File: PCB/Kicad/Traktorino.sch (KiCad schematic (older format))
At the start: 86 parts, among them J1 analog_pins, J2 mux_pins, J3 595_pins, J4 d13

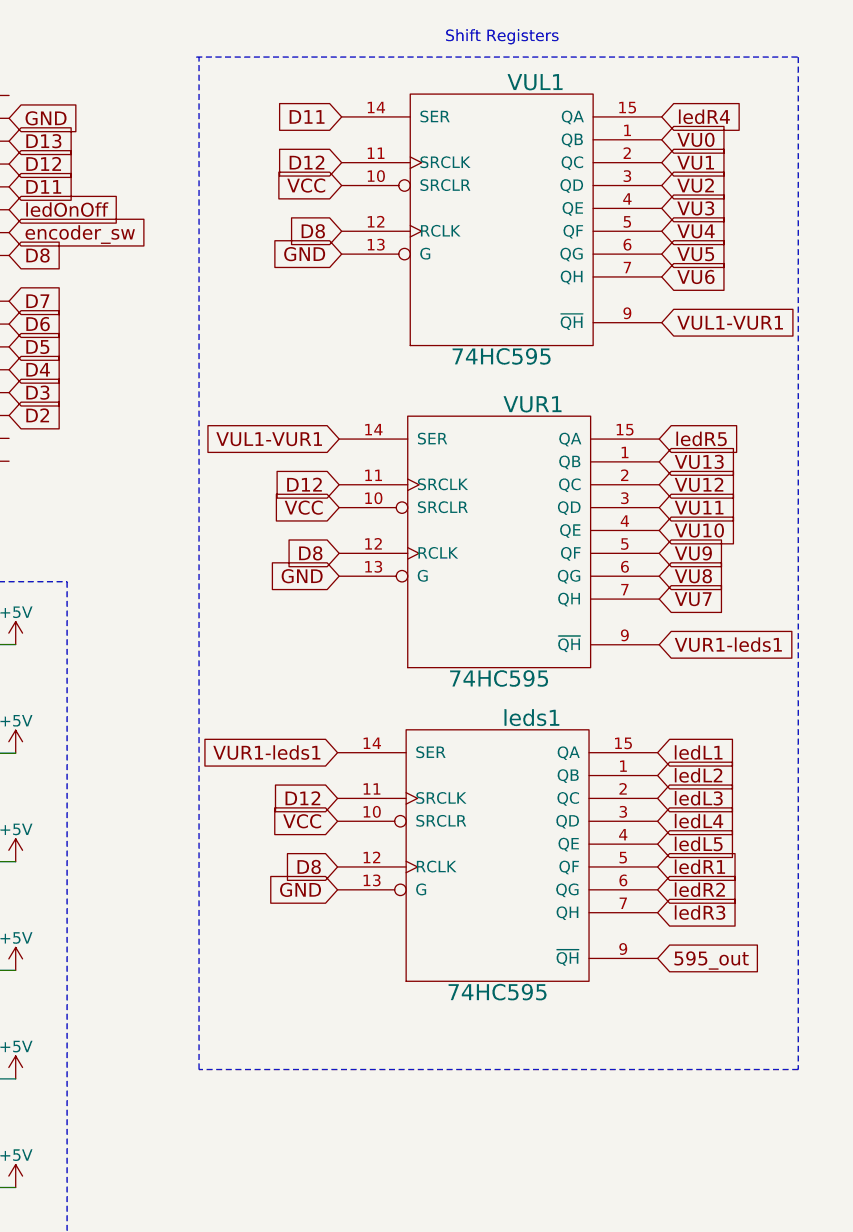
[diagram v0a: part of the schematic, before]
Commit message: SHIFT REGS
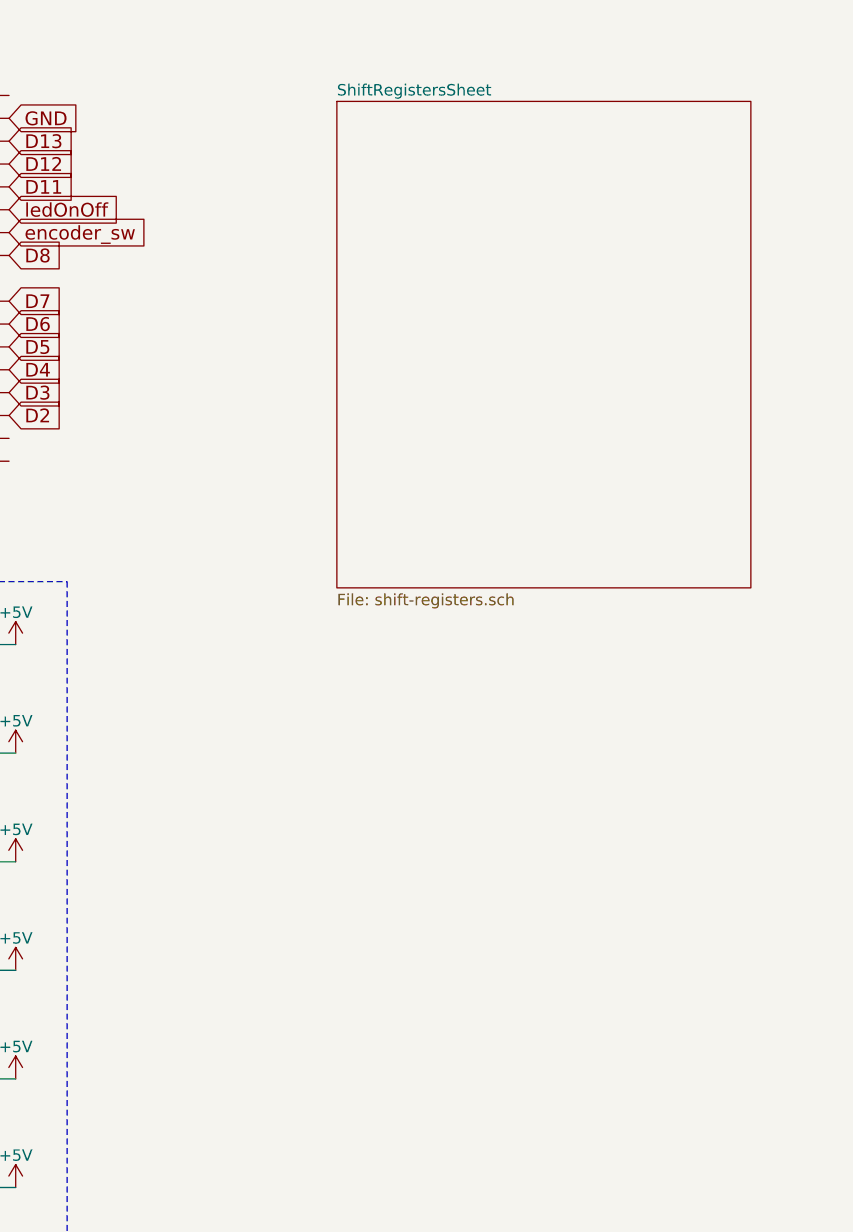
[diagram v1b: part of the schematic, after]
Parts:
- removed VUL1, VUR1, leds1: 74HC595, 74HC595:DIL16, symbol Traktorino-rescue:74HC595
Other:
- note removed: "Shift Registers"
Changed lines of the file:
@@
 $Descr A4 11693 8268
 encoding utf-8
-Sheet 1 1
+Sheet 1 2
 Title ""
 Date ""
@@
 Text GLabel 4575 6450 2    60   Input ~ 0
 Bshift
-Text GLabel 10451 1067 2    60   Input ~ 0
-VU0
-Text GLabel 10440 2976 2    60   Input ~ 0
-VU8
-Text GLabel 10440 3076 2    60   Input ~ 0
-VU7
-Text GLabel 10451 1167 2    60   Input ~ 0
-VU1
-Text GLabel 10451 1267 2    60   Input ~ 0
-VU2
-Text GLabel 10451 1367 2    60   Input ~ 0
-VU3
-Text GLabel 10451 1467 2    60   Input ~ 0
-VU4
-Text GLabel 10451 1567 2    60   Input ~ 0
-VU5
-Text GLabel 10451 1667 2    60   Input ~ 0
-VU6
-Text GLabel 10440 2876 2    60   Input ~ 0
-VU9
-Text GLabel 10440 2776 2    60   Input ~ 0
-VU10
-Text GLabel 10440 2676 2    60   Input ~ 0
-VU11
-Text GLabel 10440 2576 2    60   Input ~ 0
-VU12
-Text GLabel 10440 2476 2    60   Input ~ 0
-VU13
-Text GLabel 10433 3748 2    60   Input ~ 0
-ledL1
-Text GLabel 10433 3848 2    60   Input ~ 0
-ledL2
-Text GLabel 10433 3948 2    60   Input ~ 0
-ledL3
-Text GLabel 10433 4048 2    60   Input ~ 0
-ledL4
-Text GLabel 10433 4148 2    60   Input ~ 0
-ledL5
-Text GLabel 10433 4248 2    60   Input ~ 0
-ledR1
-Text GLabel 10433 4348 2    60   Input ~ 0
-ledR2
-Text GLabel 10433 4448 2    60   Input ~ 0
-ledR3
-Text GLabel 10451 967  2    60   Input ~ 0
-ledR4
-Text GLabel 10440 2376 2    60   Input ~ 0
-ledR5
-Text GLabel 9033 4348 0    60   Input ~ 0
-GND
-Text GLabel 9051 1467 0    60   Input ~ 0
-D8
-Text GLabel 9051 967  0    60   Input ~ 0
-D11
-Text GLabel 9051 1267 0    60   Input ~ 0
-VCC
-Text GLabel 9051 1567 0    60   Input ~ 0
-GND
 $Comp
 L Traktorino-rescue:ARDUINO_SHIELD SHIELD1
@@
 Text GLabel 5875 6850 2    60   Input ~ 0
 encoder_sw
-$Comp
-L Traktorino-rescue:74HC595 leds1
-U 1 1 5975AEC7
-P 9733 4198
-F 0 "leds1" H 9883 4798 70  0000 C CNN
-F 1 "74HC595" H 9733 3598 70  0000 C CNN
-F 2 "74HC595:DIL16" H 9733 4198 60  0001 C CNN
-F 3 "" H 9733 4198 60  0000 C CNN
-	1    9733 4198
-	1    0    0    -1
-$EndComp
-Text GLabel 9033 4248 0    60   Input ~ 0
-D8
-Text GLabel 9051 1167 0    60   Input ~ 0
-D12
-Text GLabel 9033 3948 0    60   Input ~ 0
-D12
 Text GLabel 7596 1173 2    60   Input ~ 0
 D12
-Text GLabel 9033 4048 0    60   Input ~ 0
-VCC
 Text GLabel 5696 2173 0    60   Input ~ 0
 A2
@@
 Text GLabel 5696 2473 0    60   Input ~ 0
 A5
-Text GLabel 10433 4648 2    60   Input ~ 0
-595_out
 $Comp
 L Traktorino-rescue:CONN_01X06 J2
@@
 	1    0    0    -1
 $EndComp
-Text GLabel 9040 2976 0    60   Input ~ 0
-GND
-Text GLabel 9040 2876 0    60   Input ~ 0
-D8
-Text GLabel 9040 2576 0    60   Input ~ 0
-D12
-Text GLabel 9040 2676 0    60   Input ~ 0
-VCC
 $Comp
 L Traktorino-rescue:CONN_01X07 J1
@@
 Text Notes 1750 625  0    50   ~ 0
 Multiplexers
-Text GLabel 10451 1867 2    60   Input ~ 0
-VUL1-VUR1
-Text GLabel 9040 2376 0    60   Input ~ 0
-VUL1-VUR1
-Text GLabel 10440 3276 2    60   Input ~ 0
-VUR1-leds1
-Text GLabel 9033 3748 0    60   Input ~ 0
-VUR1-leds1
-Wire Notes Line
-	8415 705  11048 705
-Wire Notes Line
-	11048 705  11048 5134
-Wire Notes Line
-	11048 5134 8427 5134
-Wire Notes Line
-	8427 5134 8427 705
-Text Notes 9503 651  0    50   ~ 0
-Shift Registers
 $Comp
 L Traktorino-rescue:SW_PUSH_SMALL BL2
@@
 Text GLabel 7596 1473 2    60   Input ~ 0
 encoder_sw
-$Comp
-L Traktorino-rescue:74HC595 VUL1
-U 1 1 59743C7D
-P 9751 1417
-F 0 "VUL1" H 9901 2017 70  0000 C CNN
-F 1 "74HC595" H 9751 817 70  0000 C CNN
-F 2 "74HC595:DIL16" H 9751 1417 60  0001 C CNN
-F 3 "" H 9751 1417 60  0000 C CNN
-	1    9751 1417
-	1    0    0    -1
-$EndComp
-$Comp
-L Traktorino-rescue:74HC595 VUR1
-U 1 1 597578F3
-P 9740 2826
-F 0 "VUR1" H 9890 3426 70  0000 C CNN
-F 1 "74HC595" H 9740 2226 70  0000 C CNN
-F 2 "74HC595:DIL16" H 9740 2826 60  0001 C CNN
-F 3 "" H 9740 2826 60  0000 C CNN
-	1    9740 2826
-	1    0    0    -1
-$EndComp
+$Sheet
+S 9030 899  1811 2128
+U 605D0BAE
+F0 "ShiftRegistersSheet" 50
+F1 "shift-registers.sch" 50
+$EndSheet
 $EndSCHEMATC

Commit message: SCHEMA UPD
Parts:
- removed MUXbuttons1, MUXpots1: 4067D, 40xx:40xx-DIL24-6, symbol Traktorino-rescue:4067D-RESCUE-DJ_0
- added SW?: SW_Push, symbol Switch:SW_Push
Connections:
- net GND: now also SW?.1
- new net SWPLAY-L: SW?.2
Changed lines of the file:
@@
 $Descr A4 11693 8268
 encoding utf-8
-Sheet 1 2
+Sheet 1 3
 Title ""
 Date ""
@@
 	1    5450 2950
 	1    0    0    -1
-$EndComp
-$Comp
-L Traktorino-rescue:4067D-RESCUE-DJ_0 MUXpots1
-U 1 1 578962B0
-P 1350 2075
-F 0 "MUXpots1" H 1050 3200 50  0000 L BNN
-F 1 "4067D" H 1050 775 50  0000 L BNN
-F 2 "40xx:40xx-DIL24-6" H 1350 2225 50  0001 C CNN
-F 3 "" H 1350 2075 60  0000 C CNN
-	1    1350 2075
-	-1   0    0    1
 $EndComp
 Text GLabel 1754 5416 2    60   Input ~ 0
@@
 Text Notes 1700 3600 0    50   ~ 0
 Vumeter
-$Comp
-L Traktorino-rescue:4067D-RESCUE-DJ_0 MUXbuttons1
-U 1 1 579016CB
-P 3050 2075
-F 0 "MUXbuttons1" H 2750 3200 50  0000 L BNN
-F 1 "4067D" H 2750 775 50  0000 L BNN
-F 2 "40xx:40xx-DIL24-6" H 3050 2225 50  0001 C CNN
-F 3 "" H 3050 2075 60  0000 C CNN
-	1    3050 2075
-	-1   0    0    1
-$EndComp
 Wire Notes Line
 	550  675  3850 675
-Wire Notes Line
-	3850 675  3850 3475
 Wire Notes Line
 	3850 3475 550  3475
@@
 Text Notes 5675 6300 0    50   ~ 0
 Browse encoder
-Text GLabel 2550 1575 0    60   Input ~ 0
-GND
-Text GLabel 2550 1725 0    60   Input ~ 0
-VCC
-Text GLabel 1850 2475 2    60   Input ~ 0
-potCF
-Text GLabel 1850 2375 2    60   Input ~ 0
-potL1
-Text GLabel 1850 2275 2    60   Input ~ 0
-potL2
-Text GLabel 1850 2175 2    60   Input ~ 0
-potL3
-Text GLabel 1850 1875 2    60   Input ~ 0
-potL6
-Text GLabel 1850 1975 2    60   Input ~ 0
-potL5
-Text GLabel 1850 2075 2    60   Input ~ 0
-potL4
-Text GLabel 1850 2675 2    60   Input ~ 0
-D7
-Text GLabel 850  1575 0    60   Input ~ 0
-GND
-Text GLabel 850  1725 0    60   Input ~ 0
-VCC
-Text GLabel 850  2475 0    60   Input ~ 0
-A0
-Text GLabel 1850 3075 2    60   Input ~ 0
-GND
-Text GLabel 1850 2975 2    60   Input ~ 0
-D4
-Text GLabel 1850 2775 2    60   Input ~ 0
-D6
-Text GLabel 1850 2875 2    60   Input ~ 0
-D5
-Text GLabel 1850 1775 2    60   Input ~ 0
-potL7
-Text GLabel 1850 1675 2    60   Input ~ 0
-potMain
-Text GLabel 1850 1575 2    60   Input ~ 0
-potR7
-Text GLabel 1850 1475 2    60   Input ~ 0
-potR6
-Text GLabel 1850 1375 2    60   Input ~ 0
-potR5
-Text GLabel 1850 1275 2    60   Input ~ 0
-potR4
-Text GLabel 1850 1175 2    60   Input ~ 0
-potR3
-Text GLabel 1850 1075 2    60   Input ~ 0
-potR2
-Text GLabel 1850 975  2    60   Input ~ 0
-potR1
-Text GLabel 2550 2475 0    60   Input ~ 0
-A1
-Text GLabel 3550 2675 2    60   Input ~ 0
-D7
-Text GLabel 3550 2775 2    60   Input ~ 0
-D6
-Text GLabel 3550 2875 2    60   Input ~ 0
-D5
-Text GLabel 3550 2975 2    60   Input ~ 0
-D4
-Text GLabel 3550 3075 2    60   Input ~ 0
-GND
-Text GLabel 3550 2475 2    60   Input ~ 0
-BL1
-Text GLabel 3550 2375 2    60   Input ~ 0
-BL2
-Text GLabel 3550 2275 2    60   Input ~ 0
-BL3
-Text GLabel 3550 2175 2    60   Input ~ 0
-BL4
-Text GLabel 3550 2075 2    60   Input ~ 0
-BL5
-Text GLabel 3550 1975 2    60   Input ~ 0
-BL6
-Text GLabel 3550 1575 2    60   Input ~ 0
-Bshift
-Text GLabel 3550 1475 2    60   Input ~ 0
-BR6
-Text GLabel 3550 1375 2    60   Input ~ 0
-BR5
-Text GLabel 3550 1275 2    60   Input ~ 0
-BR4
-Text GLabel 3550 1175 2    60   Input ~ 0
-BR3
-Text GLabel 3550 1075 2    60   Input ~ 0
-BR2
-Text GLabel 3550 975  2    60   Input ~ 0
-BR1
 Text GLabel 4650 900  0    60   Input ~ 0
 GND
@@
 F1 "shift-registers.sch" 50
 $EndSheet
+$Comp
+L Switch:SW_Push SW?
+U 1 1 605E95CD
+P 4400 7400
+F 0 "SW?" H 4400 7685 50  0000 C CNN
+F 1 "SW_Push" H 4400 7594 50  0000 C CNN
+F 2 "" H 4400 7600 50  0001 C CNN
+F 3 "~" H 4400 7600 50  0001 C CNN
+	1    4400 7400
+	1    0    0    -1
+$EndComp
+$Comp
+L power:GND #PWR?
+U 1 1 605F7A1F
+P 4100 7400
+F 0 "#PWR?" H 4100 7150 50  0001 C CNN
+F 1 "GND" H 4105 7227 50  0000 C CNN
+F 2 "" H 4100 7400 50  0001 C CNN
+F 3 "" H 4100 7400 50  0001 C CNN
+	1    4100 7400
+	1    0    0    -1
+$EndComp
+Wire Wire Line
+	4200 7400 4100 7400
+Text GLabel 4600 7400 2    40   Input ~ 0
+SWPLAY-L
+$Sheet
+S 9050 3700 1650 1450
+U 60600FDB
+F0 "MultiplexersSheet" 40
+F1 "multiplexers.sch" 40
+$EndSheet
 $EndSCHEMATC

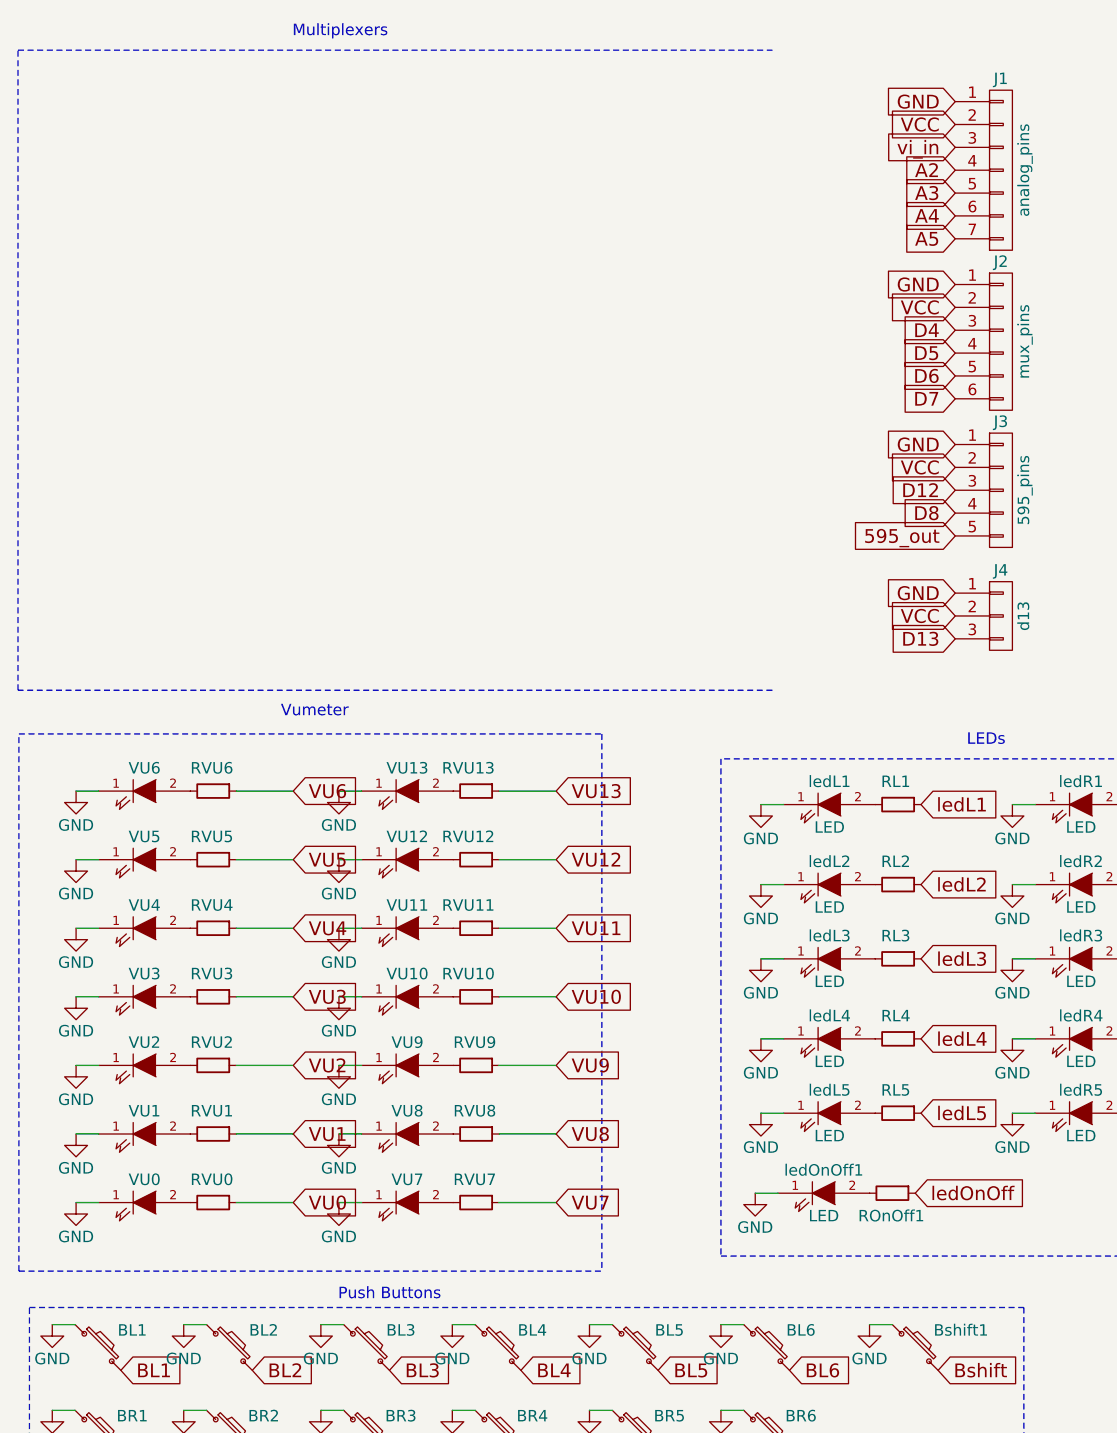
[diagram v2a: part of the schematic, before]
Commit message: multiplexers and vumeters
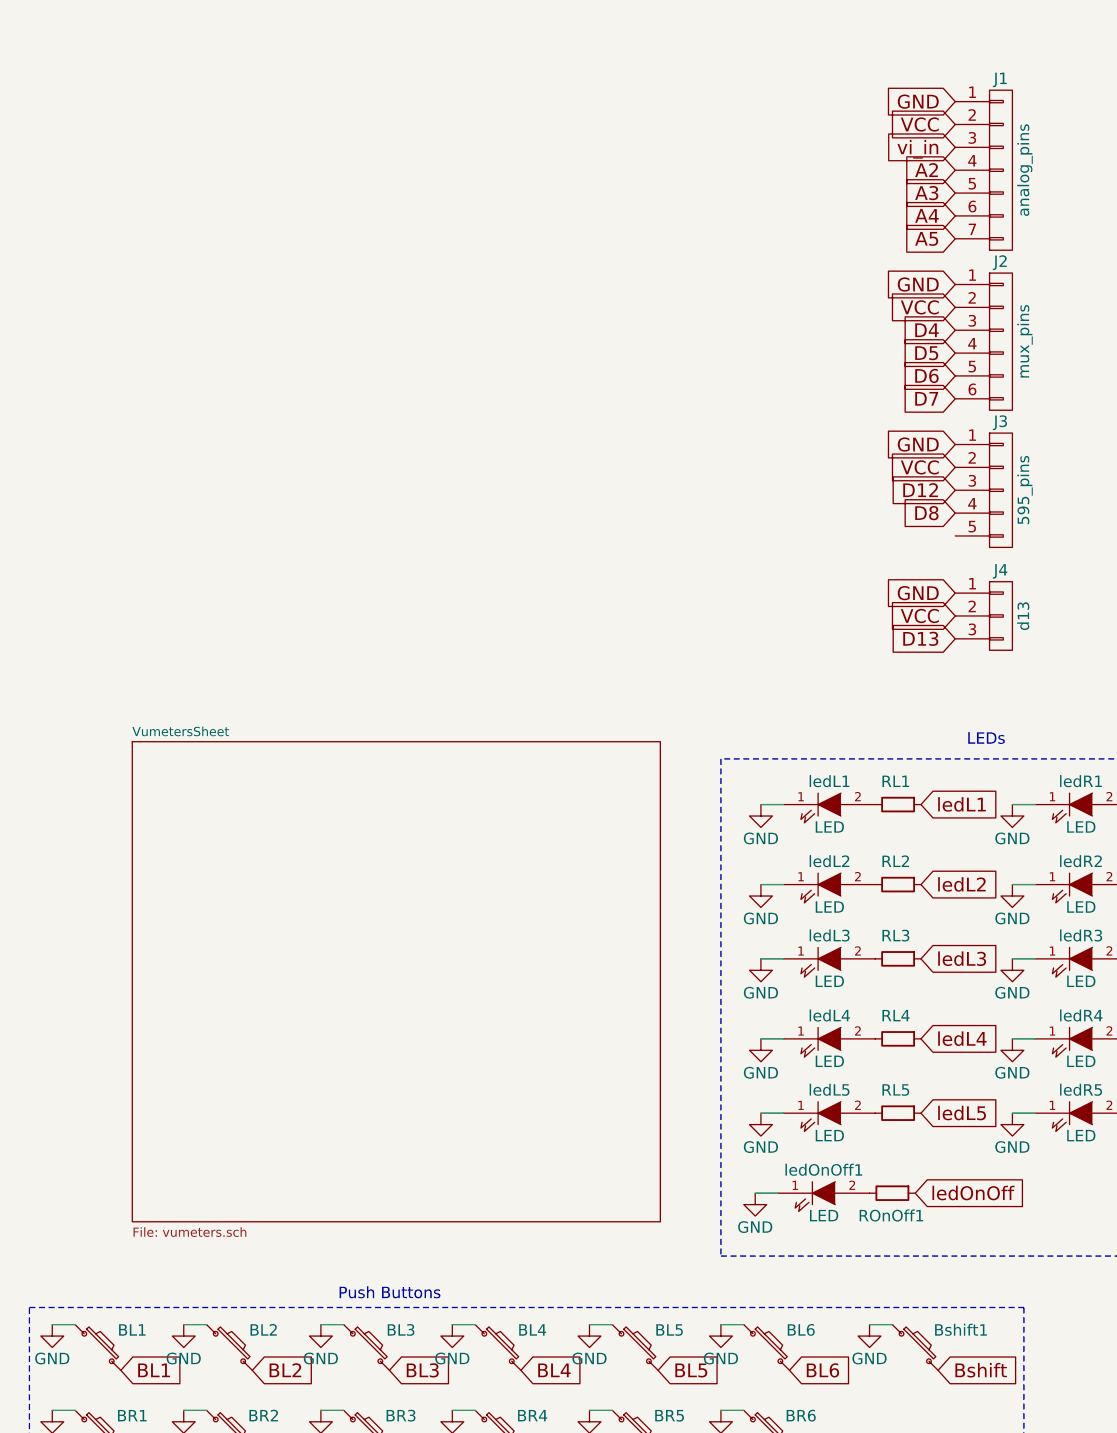
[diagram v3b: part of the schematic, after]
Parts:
- removed RVU0, RVU1, RVU10, RVU11, RVU12, RVU13, RVU2, RVU3, RVU4, RVU5, RVU6, RVU7, RVU8, RVU9: R_Small, Resistors_ThroughHole:Resistor_Horizontal_RM7mm, symbol Traktorino-rescue:R_Small
- removed VU0, VU1, VU10, VU11, VU12, VU13, VU2, VU3, VU4, VU5, VU6, VU7, VU8, VU9: LED, LEDs:LED-3MM, symbol Traktorino-rescue:LED-RESCUE-DJ_0
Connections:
- net 595_out: no longer names the net of J3.5 (P5)
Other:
- note removed: "Multiplexers"
- note removed: "Vumeter"

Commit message: more sheets
pots
vumeters
switchers
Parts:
- removed BL1, BL2, BL3, BL4, BL5, BL6, BR1, BR2, BR3, BR4, BR5, BR6, Bshift1: SW_PUSH_SMALL, Gustavo:SW_tactile, symbol Traktorino-rescue:SW_PUSH_SMALL
- removed En1: Encoder_switch, sparkfun:SF-ROTARY-ENCODER_gus, symbol Traktorino-rescue:Encoder_switch
- removed SW?: SW_Push, symbol Switch:SW_Push
- removed potL1, potL2, potL3, potL4, potL5, potL6, potR1, potR2, potR3, potR4, potR5, potR6: POT, Gustavo:Pot_vertical, symbol Traktorino-rescue:POT-RESCUE-DJ_0
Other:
- note removed: "Browse encoder"
- note removed: "Potenciometers"
- note removed: "Push Buttons"
